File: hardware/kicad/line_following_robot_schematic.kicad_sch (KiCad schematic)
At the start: 10 parts, among them J1 BATT_6V, M1 Motor_DC, M2 Motor_DC, SW1 Power Switch

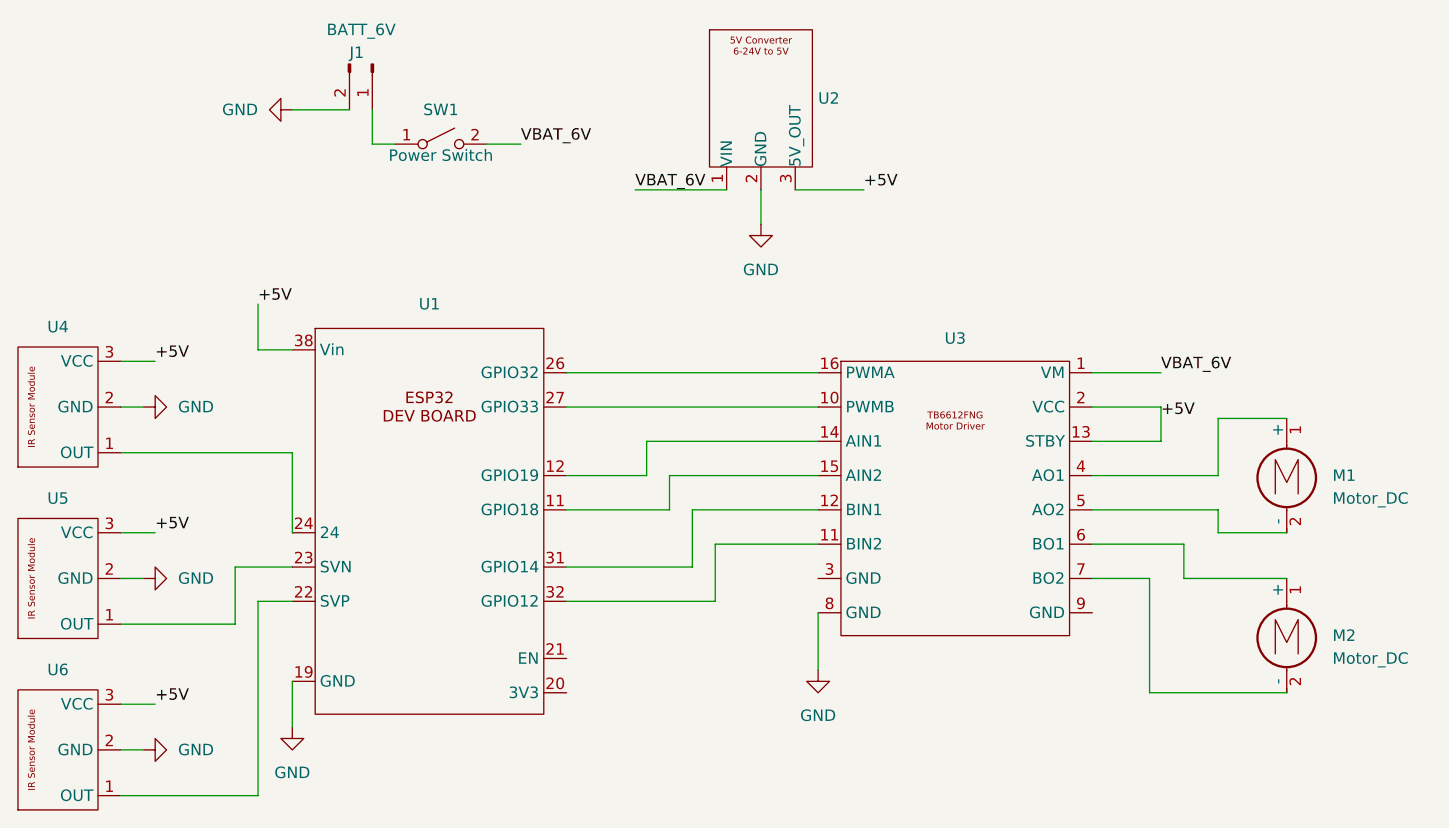
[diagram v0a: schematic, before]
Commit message: hardware: add bulk and decoupling capacitors to schematic
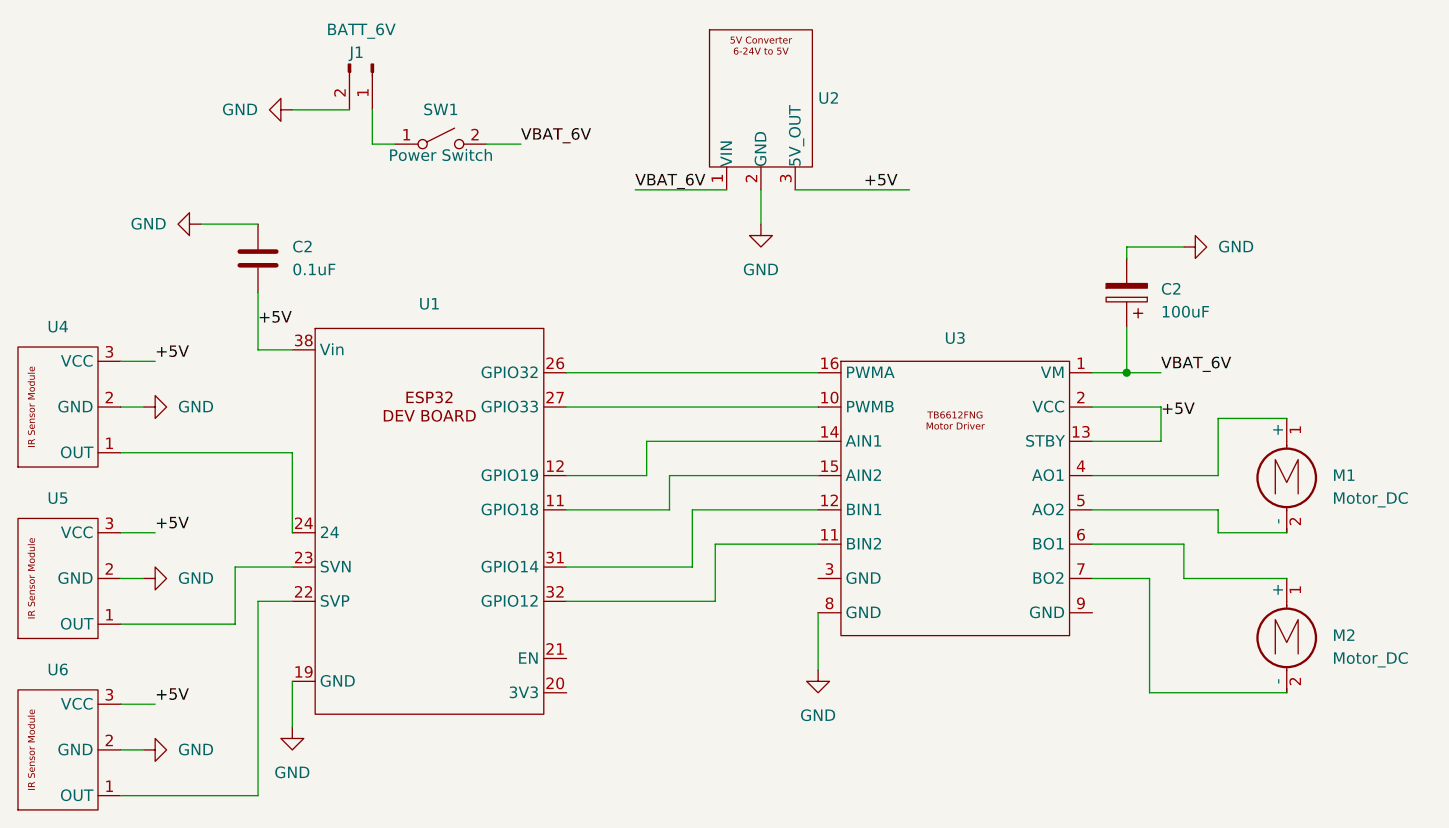
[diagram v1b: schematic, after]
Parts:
- added C2: 0.1uF, symbol Device:C
- added C2: 100uF, symbol Device:C_Polarized
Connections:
- net +5V: now also C2.2
- net GND: now also C2.1, C2.2
- net VBAT_6V: now also C2.1

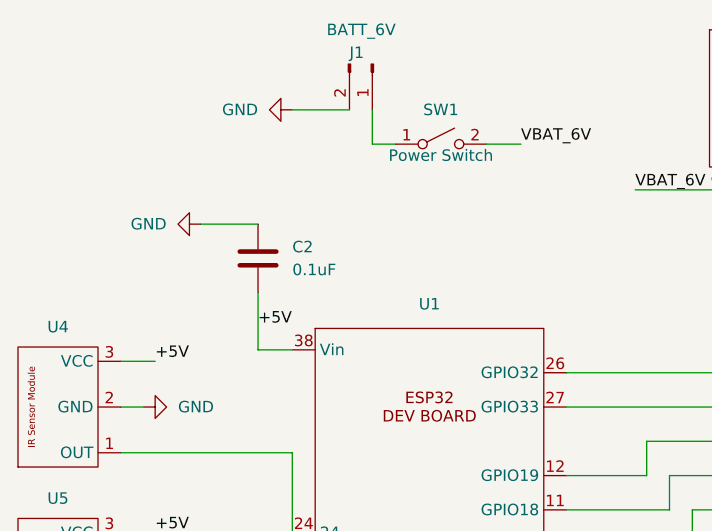
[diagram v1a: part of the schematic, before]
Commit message: test: verify motor control on perfboard with simple test logic
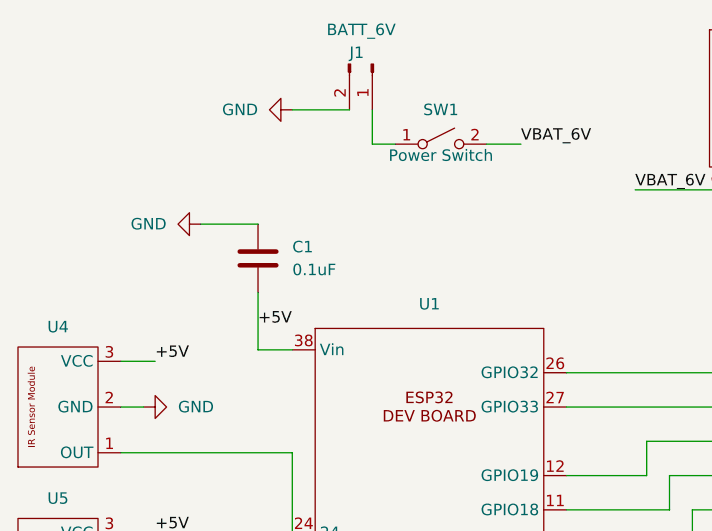
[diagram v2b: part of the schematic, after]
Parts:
- renumbered C2 to C1
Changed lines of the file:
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@@
 		(dnp no)
 		(fields_autoplaced yes)
-		(property "Reference" "C2"
+		(property "Reference" "C1"
 			(at 92.71 64.7699 0)
 			(show_name no)
@@
 			(project "line_following_robot_schematic"
 				(path "/11185b3a-932f-4897-a286-ad6ec40470ea"
-					(reference "C2")
+					(reference "C1")
 					(unit 1)
 				)
